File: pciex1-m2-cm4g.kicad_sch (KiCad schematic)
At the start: 12 parts, among them J1 Bus_M.2_Socket_M, J2 Bus_PCI_Express_x1

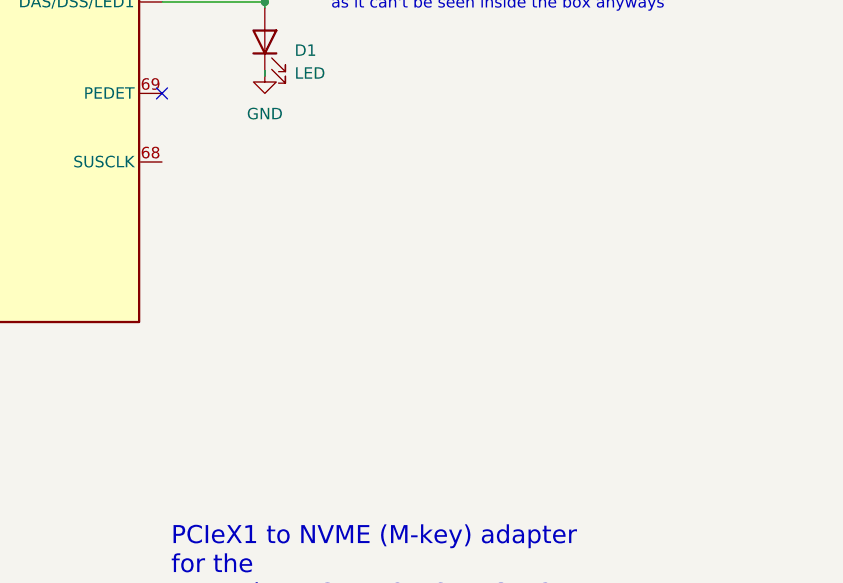
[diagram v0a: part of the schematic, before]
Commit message: added SUSClk
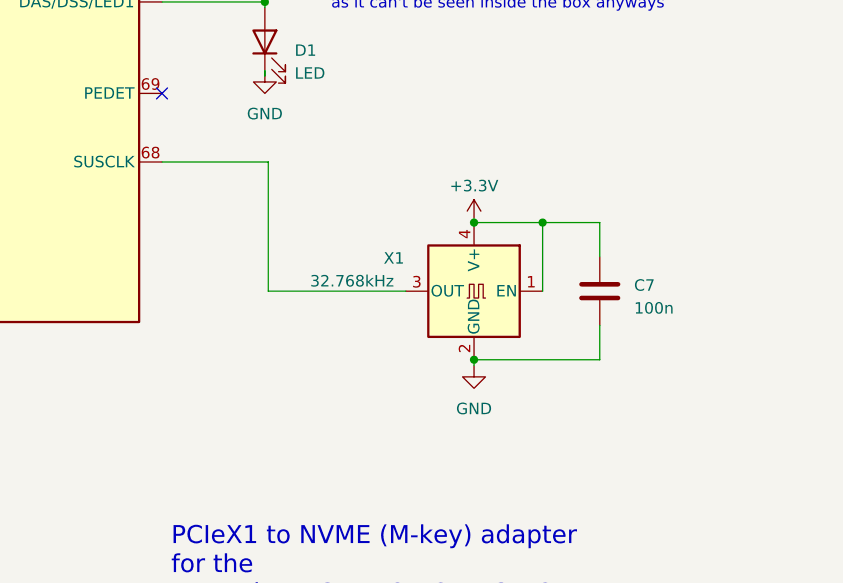
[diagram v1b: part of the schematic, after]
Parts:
- added C7: 100n, Capacitor_SMD:C_1206_3216Metric, symbol Device:C
- added X1: 32.768kHz, Oscillator:Oscillator_SMD_EuroQuartz_XO32-4Pin_3.2x2.5mm, symbol Oscillator:XO32
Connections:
- net +3.3V: now also C7.1, X1.1 (EN), X1.4 (V+)
- net GND: now also C7.2, X1.2 (GND)
- net at J1.68 (SUSCLK): now also X1.3 (OUT)
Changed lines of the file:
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@@
   (title_block
     (title "WS-CM4-PoE-4G PCIeX1 to M.2 (M) NVME adapter")
-    (date "2023-03-20")
-    (rev "0.8.2")
+    (date "2024-01-10")
+    (rev "0.9.0")
     (company "Sönke J. Peters")
   )
@@
   (junction (at 245.745 64.77) (diameter 0) (color 0 0 0 0)
   )
+  (junction (at 259.08 135.255) (diameter 0) (color 0 0 0 0)
+  )
   (junction (at 131.699 57.404) (diameter 0) (color 0 0 0 0)
   )
@@
   (junction (at 228.219 110.744) (diameter 0) (color 0 0 0 0)
   )
+  (junction (at 251.46 135.255) (diameter 0) (color 0 0 0 0)
+  )
   (junction (at 244.7379 34.29) (diameter 0) (color 0 0 0 0)
+  )
+  (junction (at 251.46 150.495) (diameter 0) (color 0 0 0 0)
   )
   (no_connect (at 216.789 120.904))
@@
     (stroke (width 0) (type default))
   )
+  (wire (pts (xy 251.46 150.495) (xy 265.43 150.495))
+    (stroke (width 0) (type default))
+  )
   (wire (pts (xy 80.899 103.124) (xy 84.201 103.124))
     (stroke (width 0) (type default))
@@
     (stroke (width 0) (type default))
   )
+  (wire (pts (xy 265.43 135.255) (xy 265.43 139.065))
+    (stroke (width 0) (type default))
+  )
   (wire (pts (xy 130.429 136.144) (xy 130.429 75.184))
     (stroke (width 0) (type default))
@@
     (stroke (width 0) (type default))
   )
+  (wire (pts (xy 259.08 135.255) (xy 265.43 135.255))
+    (stroke (width 0) (type default))
+  )
   (wire (pts (xy 235.331 64.77) (xy 245.745 64.77))
     (stroke (width 0) (type default))
@@
     (stroke (width 0) (type default))
   )
+  (wire (pts (xy 216.789 128.524) (xy 228.6 128.524))
+    (stroke (width 0) (type default))
+  )
   (wire (pts (xy 42.545 62.484) (xy 165.989 62.484))
     (stroke (width 0) (type default))
@@
     (stroke (width 0) (type default))
   )
+  (wire (pts (xy 251.46 135.255) (xy 259.08 135.255))
+    (stroke (width 0) (type default))
+  )
+  (wire (pts (xy 259.08 135.255) (xy 259.08 142.875))
+    (stroke (width 0) (type default))
+  )
   (wire (pts (xy 244.729 34.29) (xy 244.7379 34.29))
     (stroke (width 0) (type default))
   )
+  (wire (pts (xy 228.6 128.524) (xy 228.6 142.875))
+    (stroke (width 0) (type default))
+  )
   (wire (pts (xy 245.7539 57.15) (xy 256.159 57.15))
     (stroke (width 0) (type default))
@@
     (stroke (width 0) (type default))
   )
+  (wire (pts (xy 265.43 150.495) (xy 265.43 146.685))
+    (stroke (width 0) (type default))
+  )
+  (wire (pts (xy 251.46 151.13) (xy 251.46 150.495))
+    (stroke (width 0) (type default))
+  )
   (wire (pts (xy 80.899 118.364) (xy 110.363 118.364))
     (stroke (width 0) (type default))
@@
   )
   (wire (pts (xy 165.989 70.104) (xy 112.649 70.104))
+    (stroke (width 0) (type default))
+  )
+  (wire (pts (xy 228.6 142.875) (xy 243.84 142.875))
     (stroke (width 0) (type default))
   )
@@
     )
   )
+  (symbol (lib_id "power:+3.3V") (at 251.46 135.255 0) (unit 1)
+    (in_bom yes) (on_board yes) (dnp no) (fields_autoplaced)
+    (property "Reference" "#PWR020" (at 251.46 139.065 0)
+      (effects (font (size 1.27 1.27)) hide)
+    )
+    (property "Value" "+3.3V" (at 251.46 131.191 0)
+      (effects (font (size 1.27 1.27)))
+    )
+    (property "Footprint" "" (at 251.46 135.255 0)
+      (effects (font (size 1.27 1.27)) hide)
+    )
+    (property "Datasheet" "" (at 251.46 135.255 0)
+      (effects (font (size 1.27 1.27)) hide)
+    )
+    (pin "1")
+    (instances
+      (project "pciex1-m2-cm4g"
+        (path "/c3047336-7f44-463f-8e30-ba5a68ce4d54"
+          (reference "#PWR020") (unit 1)
+        )
+      )
+    )
+  )
   (symbol (lib_id "power:+3.3V") (at 131.699 43.434 0) (unit 1)
     (in_bom yes) (on_board yes) (dnp no) (fields_autoplaced)
@@
         (path "/c3047336-7f44-463f-8e30-ba5a68ce4d54"
           (reference "#PWR014") (unit 1)
+        )
+      )
+    )
+  )
+  (symbol (lib_id "Oscillator:XO32") (at 251.46 142.875 0) (mirror y) (unit 1)
+    (in_bom yes) (on_board yes) (dnp no)
+    (property "Reference" "X1" (at 242.57 139.2271 0)
+      (effects (font (size 1.27 1.27)))
+    )
+    (property "Value" "32.768kHz" (at 242.57 141.7671 0)
+      (effects (font (size 1.27 1.27)) (justify left))
+    )
+    (property "Footprint" "Oscillator:Oscillator_SMD_EuroQuartz_XO32-4Pin_3.2x2.5mm" (at 233.68 151.765 0)
+      (effects (font (size 1.27 1.27)) hide)
+    )
+    (property "Datasheet" "http://web.archive.org/web/20240108155121/https://www.jauch.com/downloadfile/57ff8a106f744_9627f8da1f8128e615cf/jro32_180618.pdf" (at 254 142.875 0)
+      (effects (font (size 1.27 1.27)) hide)
+    )
+    (property "JLCPCB" "C2901582" (at 251.46 142.875 0)
+      (effects (font (size 1.27 1.27)) hide)
+    )
+    (pin "3")
+    (pin "4")
+    (pin "2")
+    (pin "1")
+    (instances
+      (project "pciex1-m2-cm4g"
+        (path "/c3047336-7f44-463f-8e30-ba5a68ce4d54"
+          (reference "X1") (unit 1)
         )
       )
@@
         )
       )
+    )
+  )
+  (symbol (lib_id "power:GND") (at 251.46 151.13 0) (unit 1)
+    (in_bom yes) (on_board yes) (dnp no) (fields_autoplaced)
+    (property "Reference" "#PWR019" (at 251.46 157.48 0)
+      (effects (font (size 1.27 1.27)) hide)
+    )
+    (property "Value" "GND" (at 251.46 155.956 0)
+      (effects (font (size 1.27 1.27)))
+    )
+    (property "Footprint" "" (at 251.46 151.13 0)
+      (effects (font (size 1.27 1.27)) hide)
+    )
+    (property "Datasheet" "" (at 251.46 151.13 0)
+      (effects (font (size 1.27 1.27)) hide)
+    )
+    (pin "1")
+    (instances
+      (project "pciex1-m2-cm4g"
+        (path "/c3047336-7f44-463f-8e30-ba5a68ce4d54"
+          (reference "#PWR019") (unit 1)
+        )
+      )
+    )
+  )
+  (symbol (lib_id "Device:C") (at 265.43 142.875 0) (unit 1)
+    (in_bom yes) (on_board yes) (dnp no) (fields_autoplaced)
+    (property "Reference" "C7" (at 269.24 142.24 0)
+      (effects (font (size 1.27 1.27)) (justify left))
+    )
+    (property "Value" "100n" (at 269.24 144.78 0)
+      (effects (font (size 1.27 1.27)) (justify left))
+    )
+    (property "Footprint" "Capacitor_SMD:C_1206_3216Metric" (at 266.3952 146.685 0)
+      (effects (font (size 1.27 1.27)) hide)
+    )
+    (property "Datasheet" "~" (at 265.43 142.875 0)
+      (effects (font (size 1.27 1.27)) hide)
+    )
+    (pin "1")
+    (pin "2")
+    (instances
+      (project "pciex1-m2-cm4g"
+        (path "/c3047336-7f44-463f-8e30-ba5a68ce4d54"
+          (reference "C7") (unit 1)
+        )
+      )
